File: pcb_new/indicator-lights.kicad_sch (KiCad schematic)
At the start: 26 parts, among them IC1 IS31FL3236A-TQLS4-TR, J4 68021-204HLF

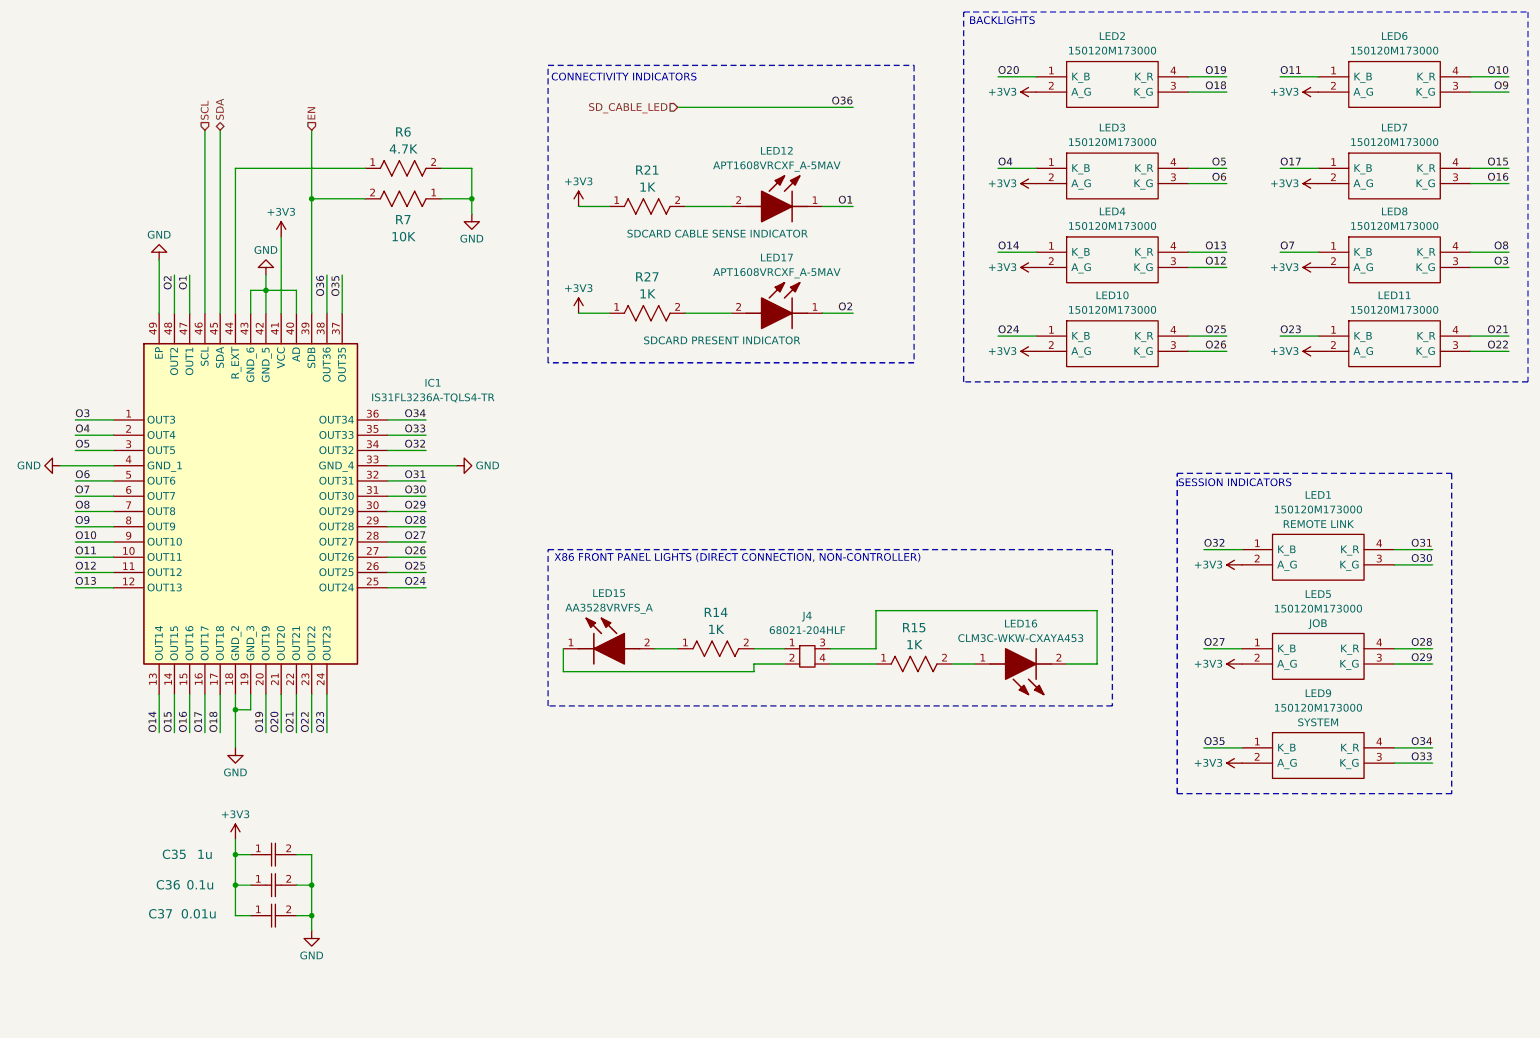
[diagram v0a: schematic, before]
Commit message: convert an RGB backlight into 3 white channels (ref #83)
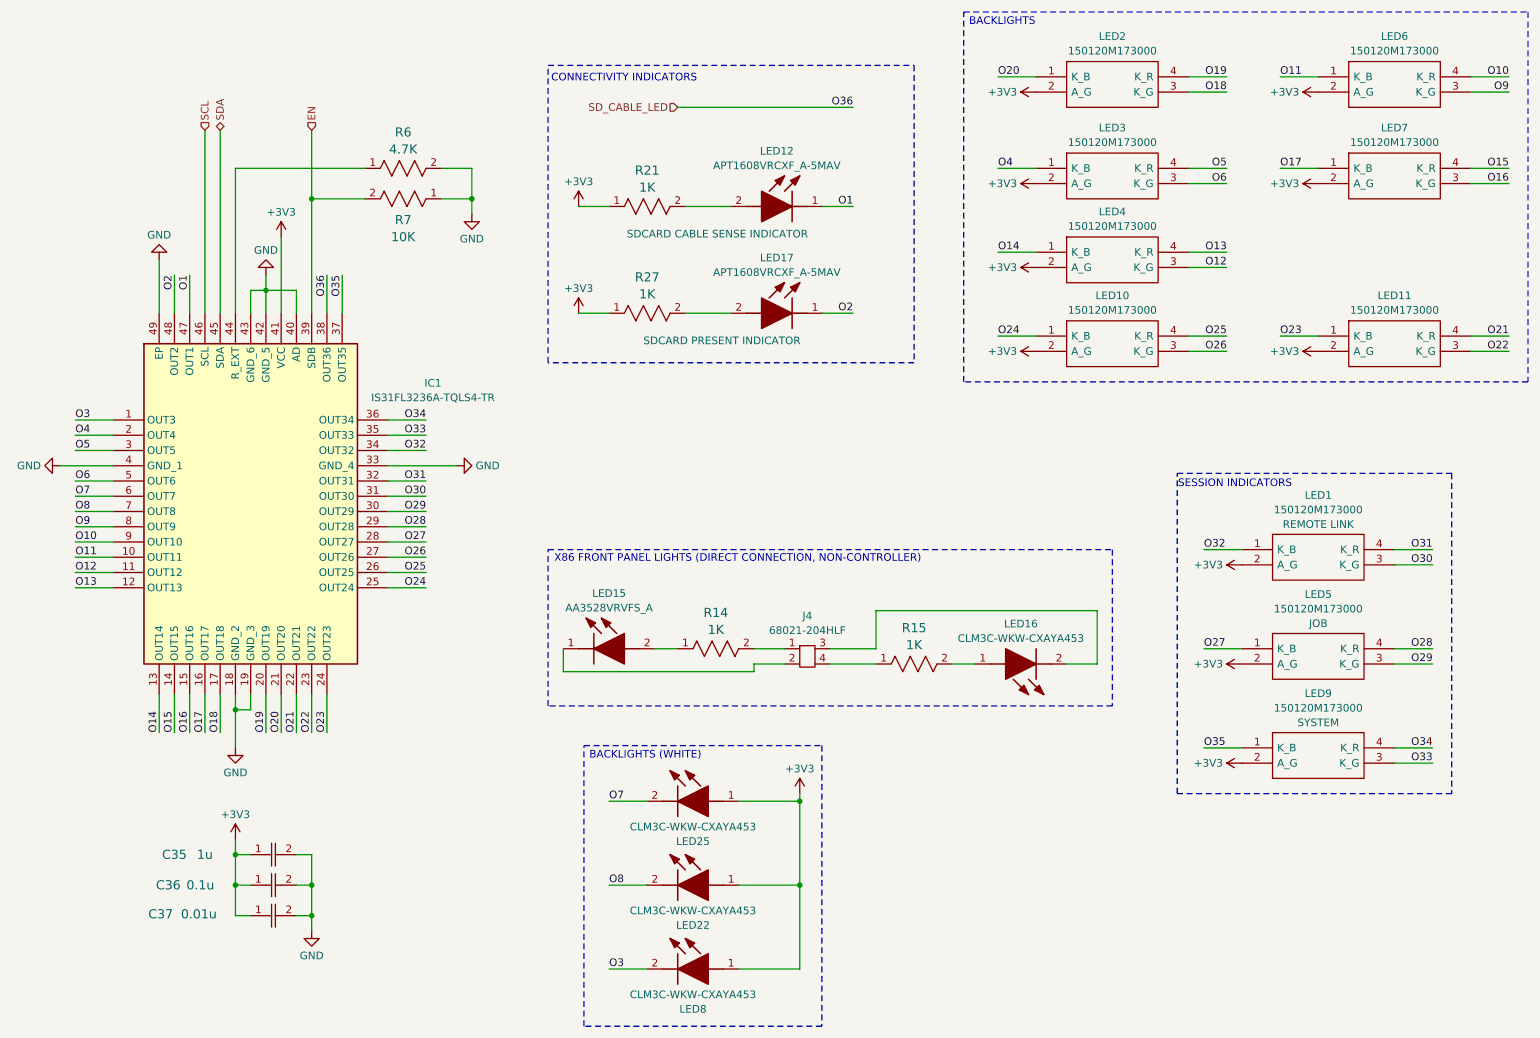
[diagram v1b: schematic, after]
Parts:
- removed LED8: 150120M173000, OroLink:150120M173000, symbol OroLink:150120M173000
- added LED22, LED25, LED8: CLM3C-WKW-CXAYA453, OroLink:CLM3CWKWCXAYA453, symbol OroLink:CLM3C-WKW-CXAYA453
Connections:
- net +3V3: now also LED22.1 (A), LED25.1 (A), LED8.1 (A)
- net O3: now also LED8.2 (K)
- net O7: now also LED25.2 (K)
- net O8: now also LED22.2 (K)
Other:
- note added: "BACKLIGHTS (WHITE)"
